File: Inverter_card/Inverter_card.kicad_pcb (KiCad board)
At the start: 2 copper layers, 156 x 80 mm, 23 parts, among them J1 CONN_01X01, J2 CONN_01X01, J3 CONN_01X01, P1 CONN_01X03, P10 CONN_01X03, P11 CONN_01X02, P2 CONN_01X03, P20 CONN_01X02, P3 CONN_01X03, P4 CONN_01X03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

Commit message: Finalized - Ready for production
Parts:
- removed the G*** at (210.4, 66.4)
- moved P1 7.50 mm to (166.6, 69.2)
- moved P3 5.47 mm to (184.7, 69.2)
- moved P10 4.70 mm to (243.7, 104.9)
- moved P5 4.46 mm to (202.7, 69.2)
- moved P6 0.27 mm to (192.8, 130.9)
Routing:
- net DC+: track 0.00 -> 346.0 mm
- net DC-: track 0.00 -> 278.1 mm
- net U: track 0.00 -> 175.1 mm, vias 0 -> 1
- net W: track 0.00 -> 158.6 mm, vias 0 -> 1
- net V: track 0.00 -> 138.9 mm, vias 0 -> 1
- net Net-(C1-Pad2): track 0.00 -> 127.9 mm
- net Net-(P11-Pad1): track 0.00 -> 105.9 mm, vias 0 -> 1
- net Net-(P11-Pad2): track 0.00 -> 101.6 mm, vias 0 -> 1
- net T1_g: track 0.00 -> 83.6 mm, vias 0 -> 1
- net T4_g: track 0.00 -> 73.3 mm, vias 0 -> 1
- net T2_g: track 0.00 -> 53.5 mm, vias 0 -> 1
- net T3_g: track 0.00 -> 52.4 mm, vias 0 -> 1
- net T6_g: track 0.00 -> 52.3 mm, vias 0 -> 1
- net T5_g: track 0.00 -> 33.2 mm, vias 0 -> 1
- net Net-(C5-Pad2): track 0.00 -> 8.46 mm
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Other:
- net class HighPower: trace_width 1.5 -> 2
- board text added: "- + Aux DC-Link Supply"
- board text added: "Inverter Connection Card rev 1"
- board text added: "It gives me a headache just trying to think down to your level."
- board text added: "T2 d g s"
- board text added: "T4 d g s"
- board text added: "T6 d g s"
- board text added: "Yngve was here"
- board text added: "s g d T1"
- board text added: "s g d T3"
- board text added: "s g d T5"
- board text removed: "Inverter Connection Card rev 1.0"
- board text removed: "T2 e g"
- board text removed: "T4 e g"
- board text removed: "T6 e g"
- board text removed: "e g T1"
- board text removed: "e g T3"
- board text removed: "e g T5"

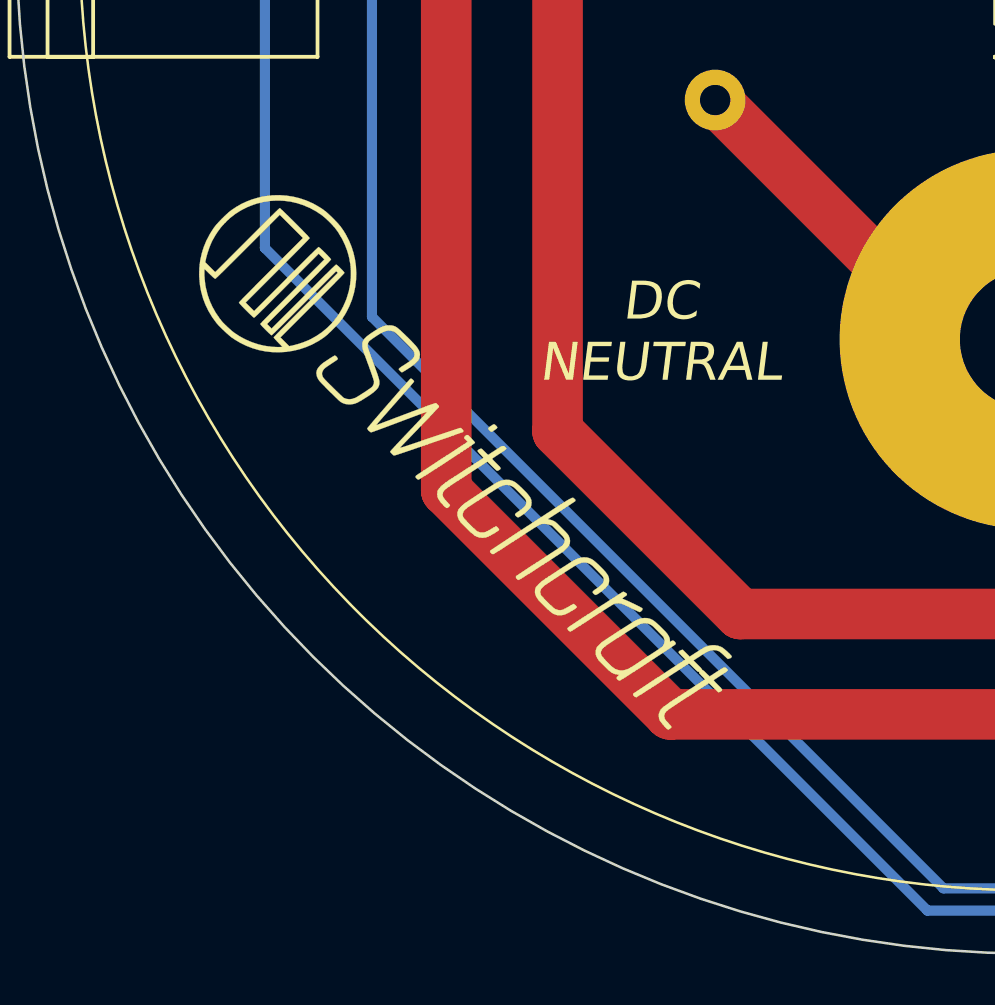
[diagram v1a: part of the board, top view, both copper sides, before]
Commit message: Added OSHW-logo
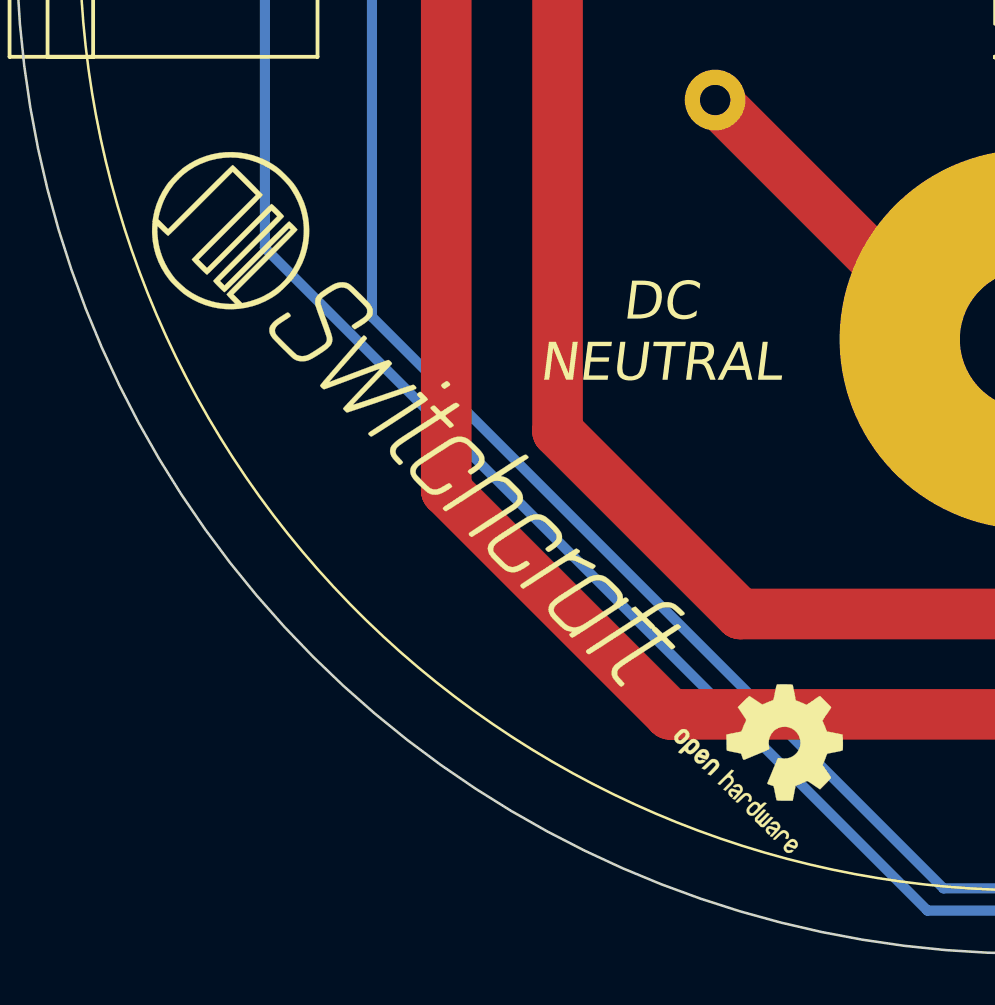
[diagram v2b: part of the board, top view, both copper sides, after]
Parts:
- added REF***: OSHW-Logo2_7.3x6mm_SilkScreen, OSHW:OSHW-Logo2_7.3x6mm_SilkScreen, F.Cu at (127.0, 132.0)
- moved G*** 2.52 mm to (113.0, 119.0)
